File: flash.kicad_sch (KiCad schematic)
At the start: 22 parts, among them J3 Socket_SOP2-16_ACA-SPI-006-K0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, J4 Socket_SOP2-16_ACA-SPI-006-K0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, U1 TLV76701_WSON, U8 TPS564247DRLR

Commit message: [#100720] Swap DCDC for LDO
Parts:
- removed C1, C2, C3, C4: C_22u_16V_0603, antmicro-footprints:C_0603_1608Metric_EIA, symbol antmicroCapacitors0603:C_22u_16V_0603
- removed C5: C_100n_0402, antmicro-footprints:C_0402_1005Metric, symbol antmicroCapacitors0402:C_100n_0402
- removed D11: LED_G_0402_VLMTG1500-GS08, antmicro-footprints:LED_0402_1005Metric_G, symbol antmicroLEDIndicationDiscrete:LED_G_0402_VLMTG1500-GS08
- removed L1: L_1u5_2.8A_0806, antmicro-footprints:L_0806_2016Metric, symbol antmicroFixedInductors:L_1u5_2.8A_0806
- removed R134: R_0R_0402, antmicro-footprints:R_0402_1005Metric, symbol antmicroResistors0402:R_0R_0402
- removed R135: R_45k3_0402, antmicro-footprints:R_0402_1005Metric, symbol antmicroResistors0402:R_45k3_0402
- removed R136, R137, R138, R139, R142: R_10k_0402, antmicro-footprints:R_0402_1005Metric, symbol antmicroResistors0402:R_10k_0402
- removed U1: TLV76701_WSON, antmicro-footprints:WSON-6-1EP_2x2mm_P0.65mm, symbol antmicroPMICVoltageRegulatorsLinear:TLV76701_WSON
- removed U8: TPS564247DRLR, antmicro-footprints:SOT-563, symbol antmicroDCDCConverters:TPS564247DRLR
- added C8, C9: C_10u_10V_0402, antmicro-footprints:C_0402_1005Metric, symbol antmicroCapacitors0402:C_10u_10V_0402
- added D3: LED_G_0402_VLMTG1500-GS08, antmicro-footprints:LED_0402_1005Metric_G, symbol antmicroLEDIndicationDiscrete:LED_G_0402_VLMTG1500-GS08
- added Q4: DMG1012T-7, antmicro-footprints:SOT-523, symbol antmicroTransistorsFETsMOSFETsSingle:DMG1012T-7
- added R143, R145: R_100k_0402, antmicro-footprints:R_0402_1005Metric, symbol antmicroResistors0402:R_100k_0402
- added R144: R_160k_0402, antmicro-footprints:R_0402_1005Metric, symbol antmicroResistors0402:R_160k_0402
- added R146: R_10k_0402, antmicro-footprints:R_0402_1005Metric, symbol antmicroResistors0402:R_10k_0402
- added R17: R_0R_22.4A_0603, antmicro-footprints:R_0603_1608Metric, symbol antmicroResistors0603:R_0R_22.4A_0603
- added U11: TLV76701_WSON, antmicro-footprints:WSON-6-1EP_2x2mm_P0.65mm, symbol antmicroPMICVoltageRegulatorsLinear:TLV76701_WSON
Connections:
- net DC_SCM_12V_AUX: now also C8.2, R146.2, U11.6 (IN)
- net DC_SCM_STBY_EN: now also U11.4 (EN)
- net GND: now also C8.1, C9.1, Q4.2 (S), R144.1, U11.3 (GND), U11.5 (GND), U11.7 (PAD)
- net +3V3 renamed +1V8
- net +1V8: now also Q4.1 (G), R17.2
- new net: R143.1, R145.2
- new net: D3.1 (C), Q4.3 (D)
- new net: D3.2 (A), R146.1
- new net 1V8_FB: R144.2, R145.1, U11.2 (FB)
- new net 1V8_R: C9.2, R143.2, R17.1, U11.1 (OUT)
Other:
- note added: "+1V8 DC/DC converter"
- note removed: "+3V3 DC/DC converter"
- note removed: "3V3 @ 1A"

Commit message: [#100720] Reannotate
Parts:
- renumbered C8 to C1, C9 to C2, C6 to C3, C7 to C4, J3 to J15, J4 to J16, Q4 to Q3, R143 to R131, R145 to R132, R144 to R133, R17 to R134, R146 to R135, R131 to R136, R132 to R137, U11 to U1

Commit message: [#100720] Finish placement
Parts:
- removed R134: R_0R_22.4A_0603, antmicro-footprints:R_0603_1608Metric, symbol antmicroResistors0603:R_0R_22.4A_0603
- added R128: R_0R_0402, antmicro-footprints:R_0402_1005Metric, symbol antmicroResistors0402:R_0R_0402
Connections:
- net +1V8: now also R128.2
- net 1V8_R: now also R128.1
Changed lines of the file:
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@@
+	)
+	(symbol
+		(lib_id "antmicroResistors0402:R_0R_0402")
+		(at 144.78 121.92 0)
+		(unit 1)
+		(body_style 1)
+		(exclude_from_sim no)
+		(in_bom yes)
+		(on_board yes)
+		(in_pos_files yes)
+		(dnp no)
+		(property "Reference" "R128"
+			(at 147.32 119.38 0)
+			(show_name no)
+			(do_not_autoplace no)
+			(effects
+				(font
+					(size 1.27 1.27)
+					(thickness 0.15)
+				)
+			)
+		)
+		(property "Value" "R_0R_0402"
+			(at 165.1 134.62 0)
+			(hide yes)
+			(show_name no)
+			(do_not_autoplace no)
+			(effects
+				(font
+					(size 1.27 1.27)
+					(thickness 0.15)
+				)
+				(justify left bottom)
+			)
+		)
+		(property "Footprint" "antmicro-footprints:R_0402_1005Metric"
+			(at 165.1 137.16 0)
+			(hide yes)
+			(show_name no)
+			(do_not_autoplace no)
+			(effects
+				(font
+					(size 1.27 1.27)
+					(thickness 0.15)
+				)
+				(justify left bottom)
+			)
+		)
+		(property "Datasheet" "https://industrial.panasonic.com/cdbs/www-data/pdf/RDA0000/AOA0000C301.pdf"
+			(at 165.1 139.7 0)
+			(hide yes)
+			(show_name no)
+			(do_not_autoplace no)
+			(effects
+				(font
+					(size 1.27 1.27)
+					(thickness 0.15)
+				)
+				(justify left bottom)
+			)
+		)
+		(property "Description" "SMD Chip Resistor, Jumper, 0 ohm, 100 mW, 0402 [1005 Metric], Thick Film, General Purpose"
+			(at 144.78 121.92 0)
+			(hide yes)
+			(show_name no)
+			(do_not_autoplace no)
+			(effects
+				(font
+					(size 1.27 1.27)
+				)
+			)
+		)
+		(property "MPN" "ERJ2GE0R00X"
+			(at 165.1 142.24 0)
+			(hide yes)
+			(show_name no)
+			(do_not_autoplace no)
+			(effects
+				(font
+					(size 1.27 1.27)
+					(thickness 0.15)
+				)
+				(justify left bottom)
+			)
+		)
+		(property "Manufacturer" "Panasonic"
+			(at 165.1 144.78 0)
+			(hide yes)
+			(show_name no)
+			(do_not_autoplace no)
+			(effects
+				(font
+					(size 1.27 1.27)
+					(thickness 0.15)
+				)
+				(justify left bottom)
+			)
+		)
+		(property "License" "Apache-2.0"
+			(at 165.1 147.32 0)
+			(hide yes)
+			(show_name no)
+			(do_not_autoplace no)
+			(effects
+				(font
+					(size 1.27 1.27)
+					(thickness 0.15)
+				)
+				(justify left bottom)
+			)
+		)
+		(property "Author" "Antmicro"
+			(at 165.1 149.86 0)
+			(hide yes)
+			(show_name no)
+			(do_not_autoplace no)
+			(effects
+				(font
+					(size 1.27 1.27)
+					(thickness 0.15)
+				)
+				(justify left bottom)
+			)
+		)
+		(property "Val" "0R"
+			(at 147.32 121.92 0)
+			(show_name no)
+			(do_not_autoplace no)
+			(effects
+				(font
+					(size 1.27 1.27)
+					(thickness 0.15)
+				)
+			)
+		)
+		(property "Tolerance" ""
+			(at 165.1 132.08 0)
+			(hide yes)
+			(show_name no)
+			(do_not_autoplace no)
+			(effects
+				(font
+					(size 1.27 1.27)
+				)
+				(justify left bottom)
+			)
+		)
+		(property "Current" "1A"
+			(at 165.1 152.4 0)
+			(hide yes)
+			(show_name no)
+			(do_not_autoplace no)
+			(effects
+				(font
+					(size 1.27 1.27)
+					(thickness 0.15)
+				)
+				(justify left bottom)
+			)
+		)
+		(pin "1"
+		)
+		(pin "2"
+		)
+		(instances
+			(project "dc-scm-server-integration-dc-scm-debug-interposer"
+				(path "/4e753ac4-580e-447a-b828-7025703de482/5a241f79-19ee-4794-a185-a01140921277"
+					(reference "R128")
+					(unit 1)
+				)
+			)
+		)
 	)
 	(symbol
@@
 					(unit 1)
 				)
-			)
-		)
-	)
-	(symbol
-		(lib_id "antmicroResistors0603:R_0R_22.4A_0603")
-		(at 144.78 121.92 0)
-		(unit 1)
-		(body_style 1)
-		(exclude_from_sim no)
-		(in_bom yes)
-		(on_board yes)
-		(in_pos_files yes)
-		(dnp no)
-		(property "Reference" "R134"
-			(at 147.32 119.38 0)
-			(show_name no)
-			(do_not_autoplace no)
-			(effects
-				(font
-					(size 1.27 1.27)
-					(thickness 0.15)
-				)
-			)
-		)
-		(property "Value" "R_0R_22.4A_0603"
-			(at 147.32 113.665 0)
-			(hide yes)
-			(show_name no)
-			(do_not_autoplace no)
-			(effects
-				(font
-					(size 1.27 1.27)
-					(thickness 0.15)
-				)
-			)
-		)
-		(property "Footprint" "antmicro-footprints:R_0603_1608Metric"
-			(at 160.02 132.08 0)
-			(hide yes)
-			(show_name no)
-			(do_not_autoplace no)
-			(effects
-				(font
-					(size 1.27 1.27)
-					(thickness 0.15)
-				)
-				(justify left bottom)
-			)
-		)
-		(property "Datasheet" "https://fscdn.rohm.com/en/products/databook/datasheet/passive/resistor/chip_resistor/pmr-jpw-e.pdf"
-			(at 160.02 134.62 0)
-			(hide yes)
-			(show_name no)
-			(do_not_autoplace no)
-			(effects
-				(font
-					(size 1.27 1.27)
-					(thickness 0.15)
-				)
-				(justify left bottom)
-			)
-		)
-		(property "Description" "SMD Chip Resistor"
-			(at 144.78 121.92 0)
-			(hide yes)
-			(show_name no)
-			(do_not_autoplace no)
-			(effects
-				(font
-					(size 1.27 1.27)
-				)
-			)
-		)
-		(property "MPN" "PMR03EZPJ000"
-			(at 160.02 137.16 0)
-			(hide yes)
-			(show_name no)
-			(do_not_autoplace no)
-			(effects
-				(font
-					(size 1.27 1.27)
-					(thickness 0.15)
-				)
-				(justify left bottom)
-			)
-		)
-		(property "Manufacturer" "ROHM Semiconductor"
-			(at 160.02 139.7 0)
-			(hide yes)
-			(show_name no)
-			(do_not_autoplace no)
-			(effects
-				(font
-					(size 1.27 1.27)
-					(thickness 0.15)
-				)
-				(justify left bottom)
-			)
-		)
-		(property "Val" "0R"
-			(at 147.32 124.46 0)
-			(show_name no)
-			(do_not_autoplace no)
-			(effects
-				(font
-					(size 1.27 1.27)
-					(thickness 0.15)
-				)
-			)
-		)
-		(property "Max. Curr." "22.4A"
-			(at 147.32 118.11 0)
-			(hide yes)
-			(show_name no)
-			(do_not_autoplace no)
-			(effects
-				(font
-					(size 1.27 1.27)
-					(thickness 0.15)
-				)
-			)
-		)
-		(property "Author" "Antmicro"
-			(at 160.02 144.78 0)
-			(hide yes)
-			(show_name no)
-			(do_not_autoplace no)
-			(effects
-				(font
-					(size 1.27 1.27)
-					(thickness 0.15)
-				)
-				(justify left bottom)
-			)
-		)
-		(property "License" "Apache-2.0"
-			(at 160.02 147.32 0)
-			(hide yes)
-			(show_name no)
-			(do_not_autoplace no)
-			(effects
-				(font
-					(size 1.27 1.27)
-					(thickness 0.15)
-				)
-				(justify left bottom)
-			)
-		)
-		(property "Tolerance" "template_tolerance"
-			(at 165.1 132.08 0)
-			(hide yes)
-			(show_name no)
-			(do_not_autoplace no)
-			(effects
-				(font
-					(size 1.27 1.27)
-				)
-				(justify left bottom)
-			)
-		)
-		(pin "2"
-		)
-		(pin "1"
-		)
-		(instances
-			(project "dc-scm-server-integration-dc-scm-debug-interposer"
-				(path "/4e753ac4-580e-447a-b828-7025703de482/5a241f79-19ee-4794-a185-a01140921277"
-					(reference "R134")
-					(unit 1)
-				)

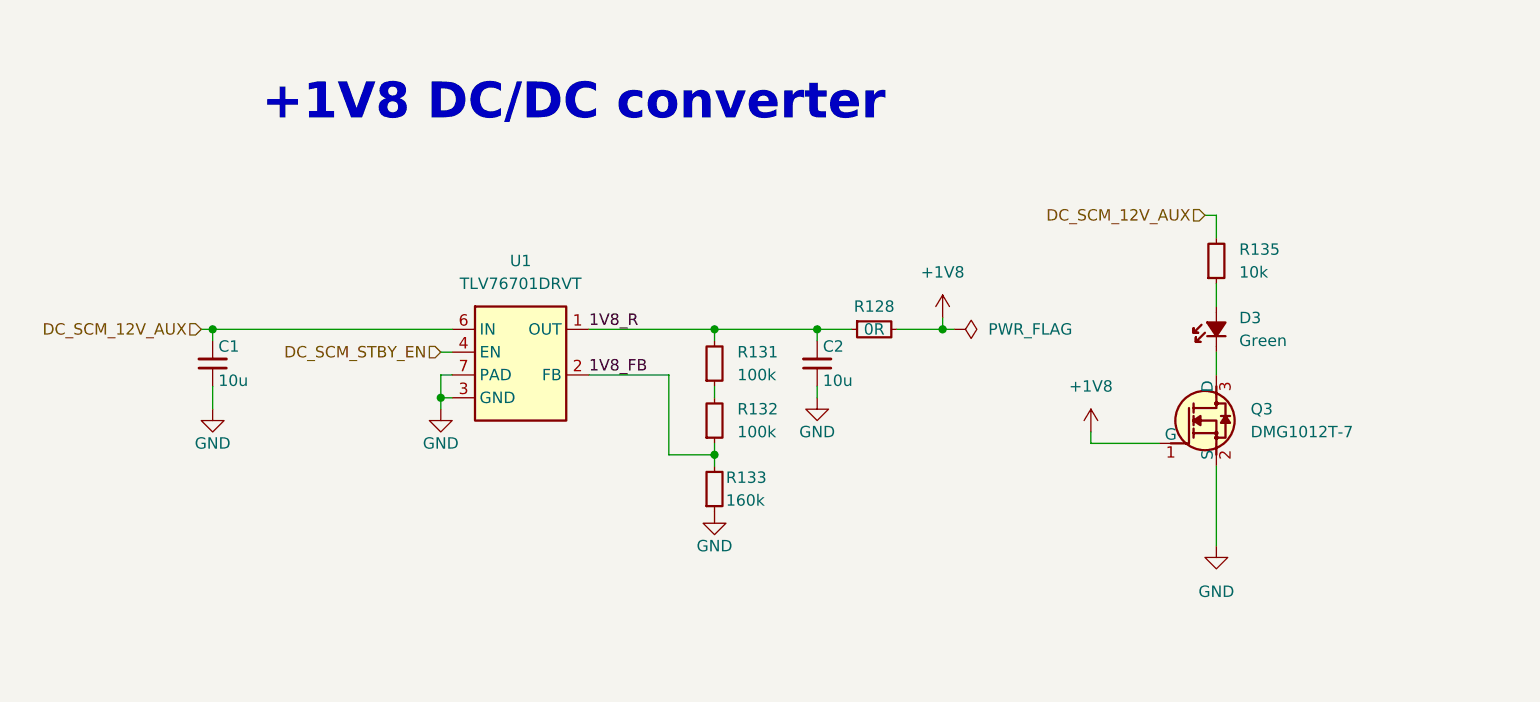
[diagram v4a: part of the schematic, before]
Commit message: [#100720] Add power section for PCIe to USB to schematic
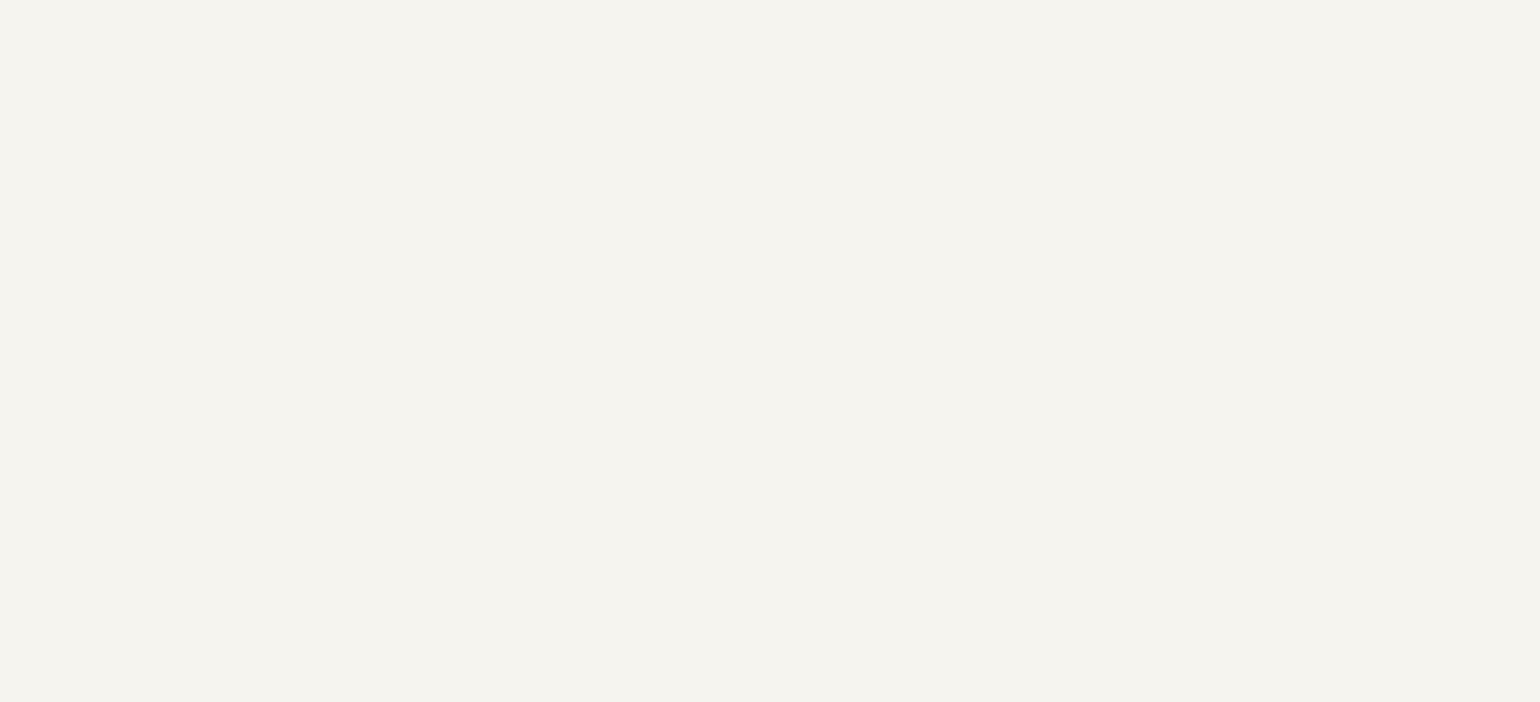
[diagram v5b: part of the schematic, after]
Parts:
- removed C1, C2: C_10u_10V_0402, antmicro-footprints:C_0402_1005Metric, symbol antmicroCapacitors0402:C_10u_10V_0402
- removed D3: LED_G_0402_VLMTG1500-GS08, antmicro-footprints:LED_0402_1005Metric_G, symbol antmicroLEDIndicationDiscrete:LED_G_0402_VLMTG1500-GS08
- removed Q3: DMG1012T-7, antmicro-footprints:SOT-523, symbol antmicroTransistorsFETsMOSFETsSingle:DMG1012T-7
- removed R128: R_0R_0402, antmicro-footprints:R_0402_1005Metric, symbol antmicroResistors0402:R_0R_0402
- removed R131, R132: R_100k_0402, antmicro-footprints:R_0402_1005Metric, symbol antmicroResistors0402:R_100k_0402
- removed R133: R_160k_0402, antmicro-footprints:R_0402_1005Metric, symbol antmicroResistors0402:R_160k_0402
- removed R135: R_10k_0402, antmicro-footprints:R_0402_1005Metric, symbol antmicroResistors0402:R_10k_0402
- removed U1: TLV76701_WSON, antmicro-footprints:WSON-6-1EP_2x2mm_P0.65mm, symbol antmicroPMICVoltageRegulatorsLinear:TLV76701_WSON
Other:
- note removed: "+1V8 DC/DC converter"

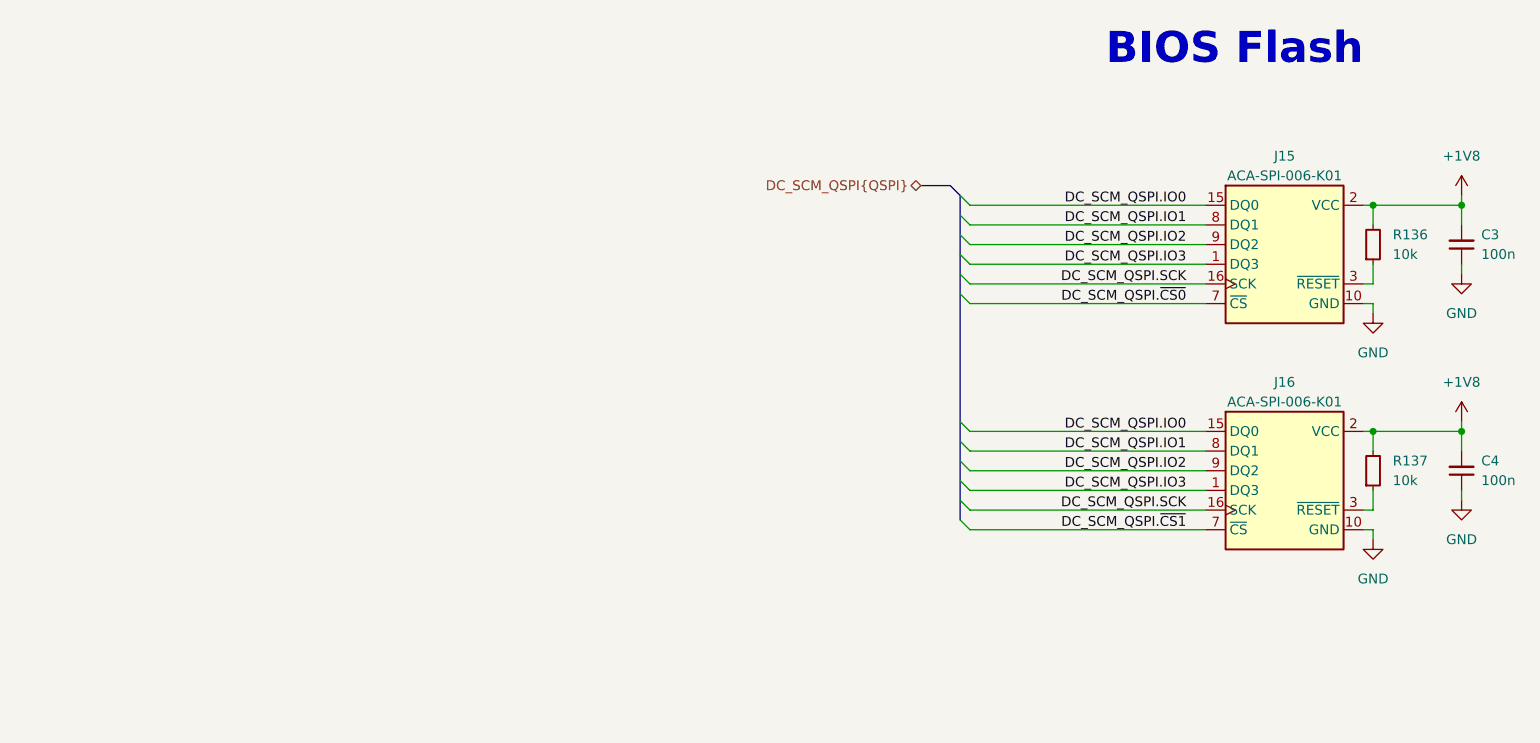
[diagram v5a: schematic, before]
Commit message: [#100720] Finish schematic after PCIe to USB addition
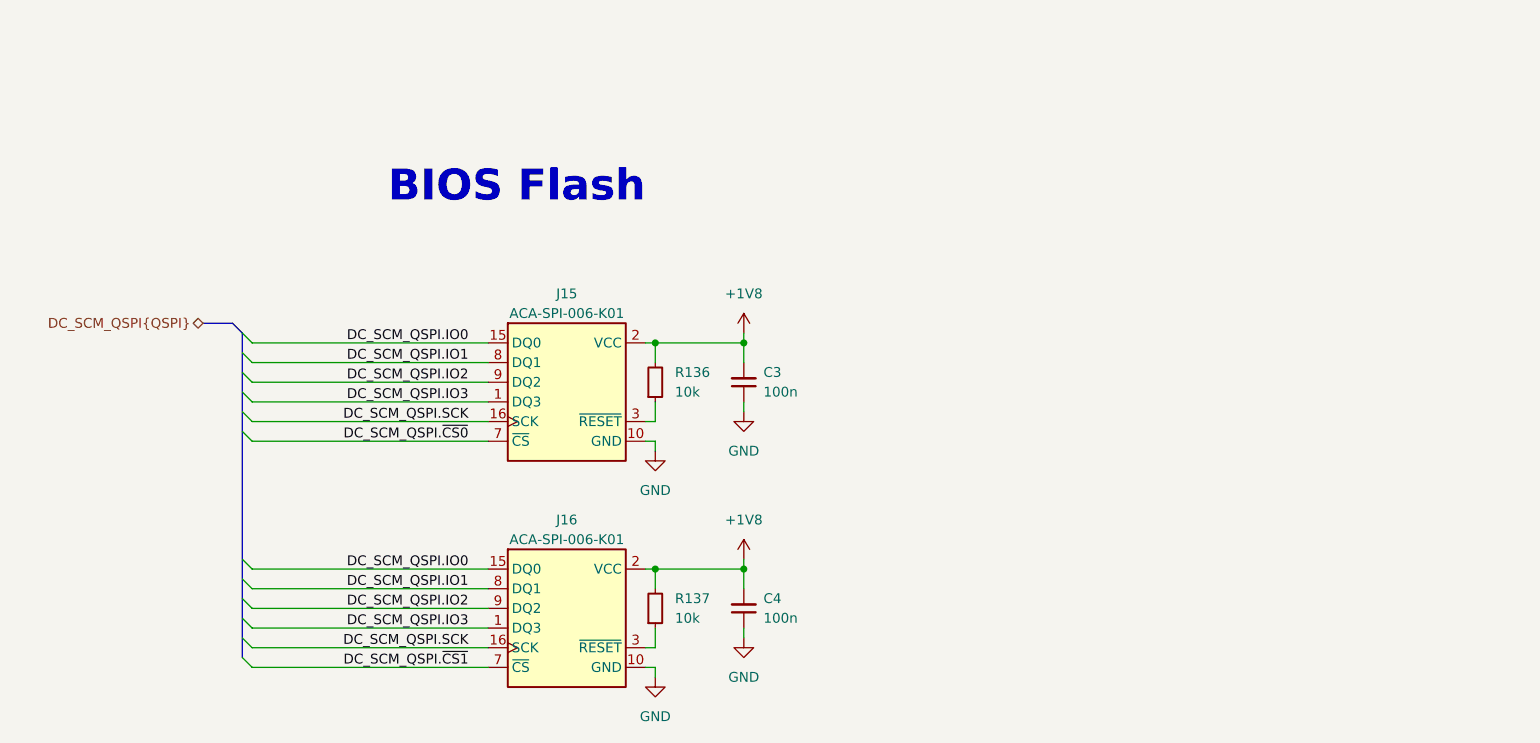
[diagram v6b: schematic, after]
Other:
- moved on the sheet: C3, C4, J15, J16, R136, R137

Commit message: [#100720] Finish placement
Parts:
- removed J15, J16: Socket_SOP2-16_ACA-SPI-006-K01_CUSTOM, antmicro-footprints:Socket_SOP2-16_ACA-SPI-006-K01, symbol antmicroMechanicalParts:Socket_SOP2-16_ACA-SPI-006-K01_CUSTOM
- added C5, C8: C_100n_0402, antmicro-footprints:C_0402_1005Metric, symbol antmicroCapacitors0402:C_100n_0402
- added J15, J16: Socket_SOP2-16_ACA-SPI-006-K01_Flash_CUSTOM, antmicro-footprints:Socket_SOP2-16_ACA-SPI-006-K01, symbol antmicroMechanicalParts:Socket_SOP2-16_ACA-SPI-006-K01_Flash_CUSTOM
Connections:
- net +1V8: now also C5.2, C8.2, J15.14 (VIO), J15.2 (VCC), J16.14 (VIO), J16.2 (VCC)
- net DC_SCM_QSPI.IO0: now also J15.15 (SI/IO0), J16.15 (SI/IO0)
- net DC_SCM_QSPI.IO1: now also J15.8 (SO/IO1), J16.8 (SO/IO1)
- net DC_SCM_QSPI.IO2: now also J15.9 (~{WP/IO2}), J16.9 (~{WP/IO2})
- net DC_SCM_QSPI.IO3: now also J15.1 (~{HOLD/IO3}), J16.1 (~{HOLD/IO3})
- net DC_SCM_QSPI.SCK: now also J15.16 (SCK), J16.16 (SCK)
- net DC_SCM_QSPI.~{CS0}: now also J16.7 (~{CS})
- net DC_SCM_QSPI.~{CS1}: now also J15.7 (~{CS})
- net GND: now also C5.1, C8.1, J15.10 (VSS), J16.10 (VSS)
- net at R137.1: now also J15.3 (~{RESET})
- net at R136.1: now also J16.3 (~{RESET})
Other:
- moved on the sheet: C3, R136

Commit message: [#100720] Clear DRC
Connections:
- net DC_SCM_QSPI.~{CS0}: now also J15.7 (~{CS}); no longer J16.7 (~{CS})
- net DC_SCM_QSPI.~{CS1}: now also J16.7 (~{CS}); no longer J15.7 (~{CS})
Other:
- moved on the sheet: C3, C4, C5, C8, J15, J16, R136, R137
